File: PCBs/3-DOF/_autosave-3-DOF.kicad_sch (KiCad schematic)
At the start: 43 parts, among them J1 Conn_02x07_Odd_Even, J10 Conn_01x06, J12 Conn_01x04, J13 Conn_01x03, J14 Conn_01x04, J15 Conn_01x04, J16 Conn_01x04, J17 Conn_01x04, J18 Conn_01x04, J2 Conn_02x08_Odd_Even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

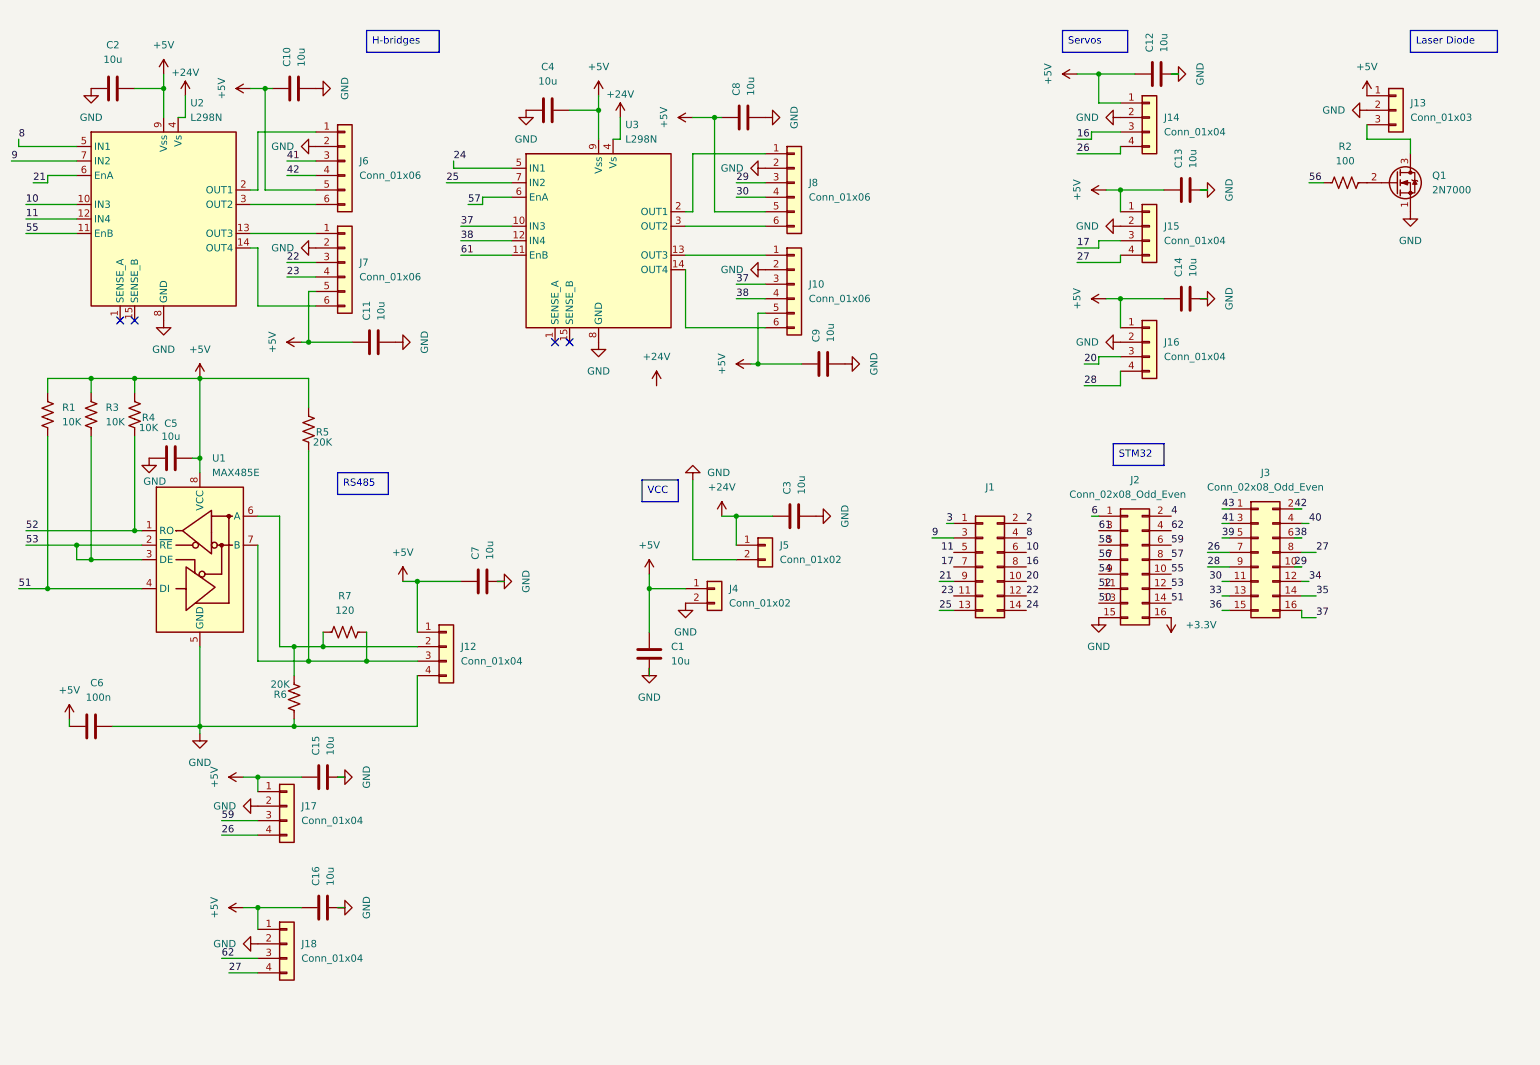
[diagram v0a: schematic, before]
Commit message: fix servos, add labels to schematic
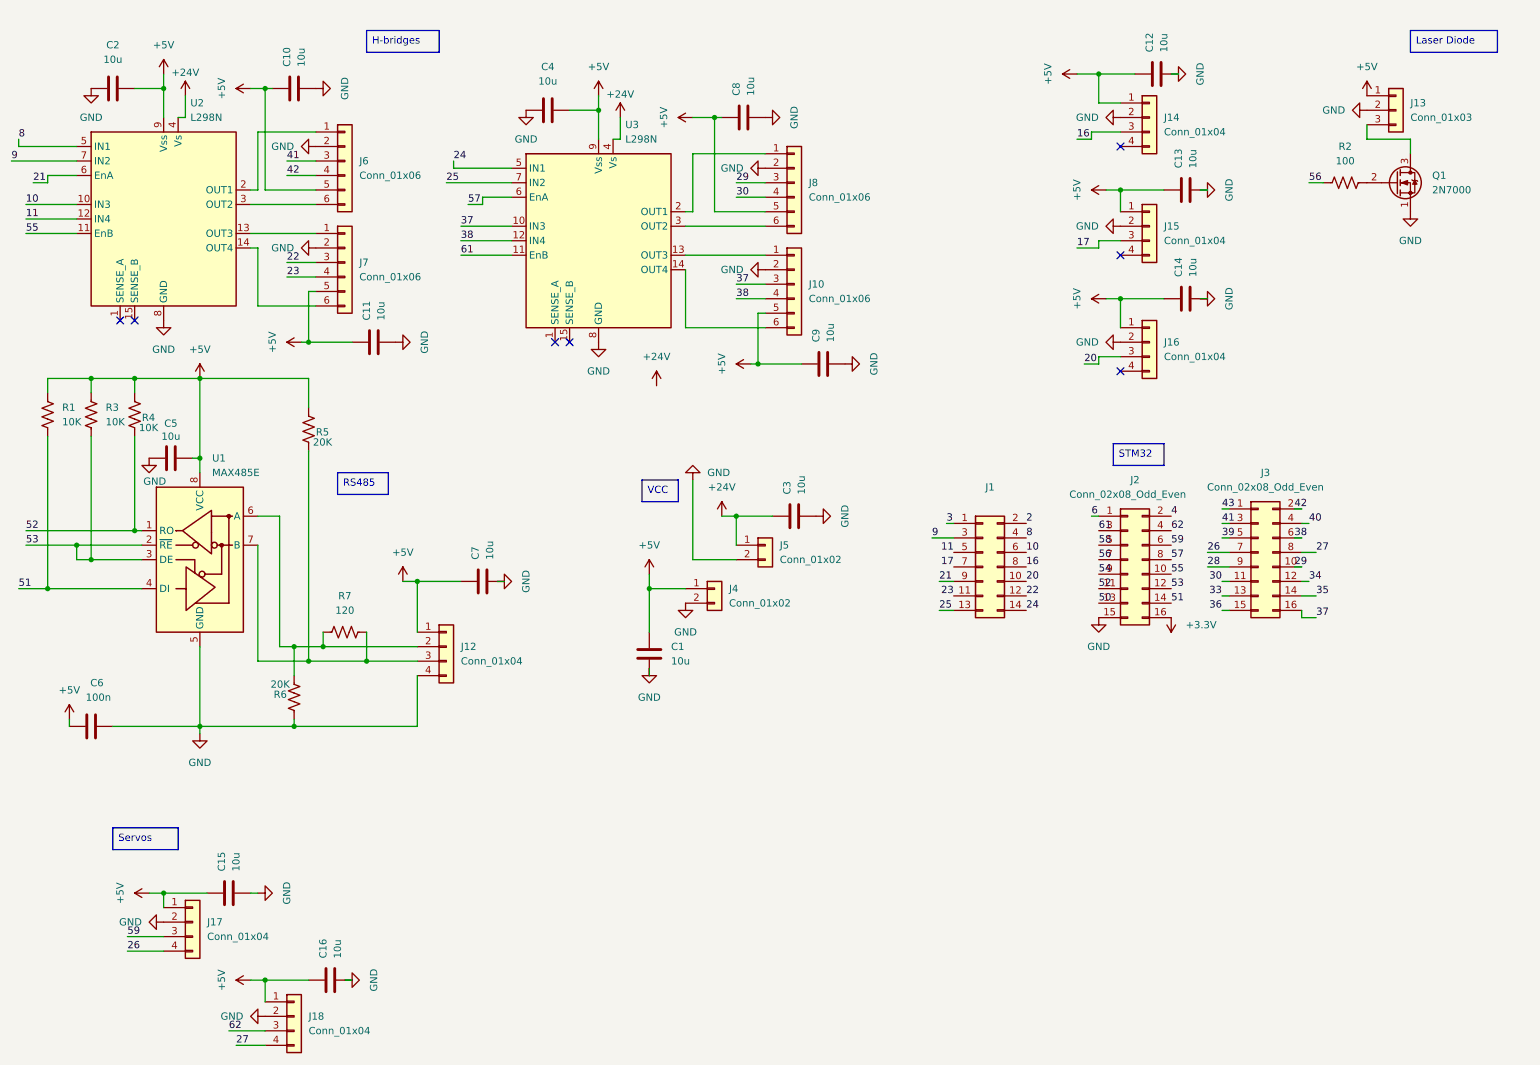
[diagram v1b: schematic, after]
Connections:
- net 26: no longer J14.4 (Pin_4)
- net 27: no longer J15.4 (Pin_4)
- net 28: no longer J16.4 (Pin_4)
- no-connect marks 4 -> 7
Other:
- moved on the sheet: C15, C16, J17, J18

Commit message: minor fixes
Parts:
- removed J13: Conn_01x03, Connector_JST:JST_XH_S3B-XH-A_1x03_P2.50mm_Horizontal, symbol Connector_Generic:Conn_01x03
- removed Q1: 2N7000, Package_TO_SOT_THT:TO-92_Inline, symbol Transistor_FET:2N7000
- removed R2: 100, Resistor_SMD:R_0402_1005Metric_Pad0.72x0.64mm_HandSolder, symbol Device:R_US
- added C17, C18: 470u, Capacitor_SMD:C_0402_1005Metric_Pad0.74x0.62mm_HandSolder, symbol Device:C
- added J9: Conn_01x02, symbol Connector_Generic:Conn_01x02
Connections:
- net +24V: now also C17.2, C18.2
- net +5V: now also J17.2 (Pin_2), J18.2 (Pin_2); no longer J17.1 (Pin_1), J18.1 (Pin_1)
- net 56: now also J9.1 (Pin_1)
- net GND: now also J17.1 (Pin_1), J18.1 (Pin_1), U2.1 (SENSE_A), U2.15 (SENSE_B), U3.1 (SENSE_A), U3.15 (SENSE_B), C17.1, C18.1, J9.2 (Pin_2); no longer J17.2 (Pin_2), J18.2 (Pin_2)
- no-connect marks 7 -> 3
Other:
- moved on the sheet: C15, J17, J18
